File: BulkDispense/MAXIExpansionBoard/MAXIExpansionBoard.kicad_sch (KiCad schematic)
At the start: 25 parts, among them J1 BS1~4, J10 FS3, J11 R6~R7, J12 R8~R9, J13 OS1~4, J14 WV1~2, J15 FS2, J16 FS4, J17 Analog Inputs, J18 Digital IN + R0~R4, J19 Digital Outputs, J2 MV1~4, J20 R4~R9, J21 Flow Sensors, J3 WB/WL, J4 PS/PCV, J5 Screw_Terminal_01x02, J6 R0~R1, J7 R2~R3, J8 R4~R5, J9 FS1

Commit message: Design Overhaul
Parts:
- removed J1: BS1~4, PartsLibrary:CONN_37204-62A3-004PL_3MM, symbol Connector:Conn_01x04_Socket
- removed J10: FS3, PartsLibrary:CONN_37204-62A3-004PL_3MM, symbol Connector:Conn_01x04_Socket
- removed J13: OS1~4, PartsLibrary:CONN_37204-62A3-004PL_3MM, symbol Connector:Conn_01x04_Socket
- removed J14: WV1~2, PartsLibrary:3720362A3003PL, symbol Connector:Conn_01x03_Socket
- removed J17: Analog Inputs, PartsLibrary:CONN_37212-62M3-003PL_3MM, symbol Connector:Conn_01x12_Socket
- removed J19: Digital Outputs, PartsLibrary:CONN_37212-62M3-003PL_3MM, symbol Connector:Conn_01x12_Socket
- removed J2: MV1~4, PartsLibrary:CONN_37204-62A3-004PL_3MM, symbol Connector:Conn_01x04_Socket
- removed J3: WB/WL, PartsLibrary:CONN_37204-62A3-004PL_3MM, symbol Connector:Conn_01x04_Socket
- removed J4: PS/PCV, PartsLibrary:3720362A3003PL, symbol Connector:Conn_01x03_Socket
- removed J5: Screw_Terminal_01x02, PartsLibrary:691137710002, symbol Connector:Screw_Terminal_01x02
- removed J6: R0~R1, PartsLibrary:CONN_37204-62A3-004PL_3MM, symbol Connector:Conn_01x04_Socket
- removed J7: R2~R3, PartsLibrary:CONN_37204-62A3-004PL_3MM, symbol Connector:Conn_01x04_Socket
- removed J8: R4~R5, PartsLibrary:CONN_37204-62A3-004PL_3MM, symbol Connector:Conn_01x04_Socket
- added H10, H5, H6, H7, H8, H9: MountingHole, MountingHole:MountingHole_2.5mm, symbol Mechanical:MountingHole
- added H11: MountingHole, MountingHole:MountingHole_3.2mm_M3, symbol Mechanical:MountingHole
- added J13: PS/PCV, PartsLibrary:3720362A3003PL, symbol Connector:Conn_01x03_Socket
- added J14: RV1&2, PartsLibrary:CONN_37204-62A3-004PL_3MM, symbol Connector:Conn_01x04_Socket
- added J17: FS3, PartsLibrary:CONN_37204-62A3-004PL_3MM, symbol Connector:Conn_01x04_Socket
- added J18: WB-MV1~4, PartsLibrary:CONN_37204-62A3-004PL_3MM, symbol Connector:Conn_01x04_Socket
- added J19: FS2, PartsLibrary:CONN_37204-62A3-004PL_3MM, symbol Connector:Conn_01x04_Socket
- added J2: BS1~4, PartsLibrary:CONN_37212-62M3-003PL_3MM, symbol Connector:Conn_01x12_Socket
- added J20: FS4, PartsLibrary:CONN_37204-62A3-004PL_3MM, symbol Connector:Conn_01x04_Socket
- added J21: BS1~4, PartsLibrary:CONN_37204-62A3-004PL_3MM, symbol Connector:Conn_01x04_Socket
- added J22: OS1~4, PartsLibrary:CONN_37204-62A3-004PL_3MM, symbol Connector:Conn_01x04_Socket
- added J23: WB-MV5~6, PartsLibrary:CONN_37204-62A3-004PL_3MM, symbol Connector:Conn_01x04_Socket
- added J3: Screw_Terminal_01x02, PartsLibrary:691137710002, symbol Connector:Screw_Terminal_01x02
- added J4: DigitalOUT 0~3, PartsLibrary:CONN_37204-62A3-004PL_3MM, symbol Connector:Conn_01x04_Socket
- added J5: DigitalOUT 4~7, PartsLibrary:CONN_37204-62A3-004PL_3MM, symbol Connector:Conn_01x04_Socket
- added J6: OS1~4, PartsLibrary:CONN_37212-62M3-003PL_3MM, symbol Connector:Conn_01x12_Socket
- added J8: Fan PWR, PartsLibrary:3720362A3003PL, symbol Connector:Conn_01x03_Socket
- H1, H2, H3, H4: footprint MountingHole:MountingHole_2.2mm_M2 -> MountingHole:MountingHole_3.2mm_M3
- J1: renamed from J18; value Digital IN + R0~R4 -> R0~R5
- J10: renamed from J21; value Flow Sensors -> FS2~FS4
- J11: value R6~R7 -> MV1~4
- J12: value R8~R9 -> WB/WL
- J15: value FS2 -> RV3&4
- J16: value FS4 -> FS1
- J7: renamed from J20; value R4~R9 -> AnalogIOs
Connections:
- net +24V: now also J7.10 (Pin_10), J2.1 (Pin_1), J2.10 (Pin_10), J2.4 (Pin_4), J2.7 (Pin_7), J3.1 (Pin_1), J6.1 (Pin_1), J6.10 (Pin_10), J6.4 (Pin_4), J6.7 (Pin_7), J8.1 (Pin_1)
- net AI0: now also J2.3 (Pin_3), J21.1 (Pin_1)
- net AI1: now also J2.6 (Pin_6), J21.2 (Pin_2)
- net AI12: now also J7.5 (Pin_5), J13.1 (Pin_1)
- net AI13: now also J7.6 (Pin_6), J13.2 (Pin_2)
- net AI2: now also J2.9 (Pin_9), J21.3 (Pin_3)
- net AI3: now also J2.12 (Pin_12), J21.4 (Pin_4)
- net AI4: now also J12.1 (Pin_1), J7.1 (Pin_1)
- net AI5: now also J12.2 (Pin_2), J7.2 (Pin_2)
- net AI6: now also J12.3 (Pin_3), J7.3 (Pin_3)
- net AI7: now also J12.4 (Pin_4), J7.4 (Pin_4)
- net AO0: now also J7.8 (Pin_8), J13.3 (Pin_3); no longer J10.11 (Pin_11)
- net DI0: now also J22.1 (Pin_1), J6.3 (Pin_3); no longer J1.1 (Pin_1)
- net DI1: now also J22.2 (Pin_2), J6.6 (Pin_6); no longer J1.2 (Pin_2)
- net DI2: now also J22.3 (Pin_3), J6.9 (Pin_9); no longer J1.3 (Pin_3)
- net DI3: now also J22.4 (Pin_4), J6.12 (Pin_12); no longer J1.4 (Pin_4)
- net DO0: now also J11.1 (Pin_1), J4.1 (Pin_1)
- net DO1: now also J11.2 (Pin_2), J4.2 (Pin_2)
- net DO2: now also J11.3 (Pin_3), J4.3 (Pin_3)
- net DO3: now also J11.4 (Pin_4), J4.4 (Pin_4)
- net FS1-1: now also J16.1 (Pin_1)
- net FS1-2: now also J16.2 (Pin_2)
- net FS1-3: now also J16.3 (Pin_3)
- net FS1-4: now also J16.4 (Pin_4)
- net FS2-1: now also J10.1 (Pin_1), J19.1 (Pin_1); no longer J15.1 (Pin_1)
- net FS2-2: now also J10.2 (Pin_2), J19.2 (Pin_2); no longer J15.2 (Pin_2)
- net FS2-3: now also J10.3 (Pin_3), J19.3 (Pin_3); no longer J10.1 (Pin_1), J15.3 (Pin_3)
- net FS2-4: now also J10.4 (Pin_4), J19.4 (Pin_4); no longer J10.2 (Pin_2), J15.4 (Pin_4)
- net FS3-1: now also J10.5 (Pin_5), J17.1 (Pin_1); no longer J10.3 (Pin_3)
- net FS3-2: now also J10.6 (Pin_6), J17.2 (Pin_2); no longer J10.4 (Pin_4)
- net FS3-3: now also J10.7 (Pin_7), J17.3 (Pin_3); no longer J10.5 (Pin_5)
- net FS3-4: now also J10.8 (Pin_8), J17.4 (Pin_4); no longer J10.6 (Pin_6)
- net FS4-1: now also J10.9 (Pin_9), J20.1 (Pin_1); no longer J10.7 (Pin_7), J16.1 (Pin_1)
- net FS4-2: now also J10.10 (Pin_10), J20.2 (Pin_2); no longer J10.8 (Pin_8), J16.2 (Pin_2)
- net FS4-3: now also J10.11 (Pin_11), J20.3 (Pin_3); no longer J10.9 (Pin_9), J16.3 (Pin_3)
- net FS4-4: now also J10.12 (Pin_12), J20.4 (Pin_4); no longer J10.10 (Pin_10), J16.4 (Pin_4)
- net GND: now also J7.12 (Pin_12), J2.11 (Pin_11), J2.2 (Pin_2), J2.5 (Pin_5), J2.8 (Pin_8), J3.2 (Pin_2), J6.11 (Pin_11), J6.2 (Pin_2), J6.5 (Pin_5), J6.8 (Pin_8)
- net R0_IN: now also J1.1 (Pin_1), J14.2 (Pin_2); no longer J1.5 (Pin_5)
- net R0_OUT: now also J1.7 (Pin_7), J14.1 (Pin_1); no longer J1.9 (Pin_9)
- net R1_IN: now also J1.2 (Pin_2), J14.4 (Pin_4); no longer J1.6 (Pin_6)
- net R1_OUT: now also J1.8 (Pin_8), J14.3 (Pin_3); no longer J1.10 (Pin_10)
- net R2_IN: now also J1.3 (Pin_3), J15.2 (Pin_2); no longer J1.7 (Pin_7)
- net R2_OUT: now also J1.9 (Pin_9), J15.1 (Pin_1); no longer J1.11 (Pin_11)
- net R3_IN: now also J1.4 (Pin_4), J15.4 (Pin_4); no longer J1.8 (Pin_8)
- net R3_OUT: now also J1.10 (Pin_10), J15.3 (Pin_3); no longer J1.12 (Pin_12)
- net R4_IN: now also J1.5 (Pin_5), J23.2 (Pin_2); no longer J7.1 (Pin_1)
- net R4_OUT: now also J1.11 (Pin_11), J23.1 (Pin_1); no longer J7.7 (Pin_7)
- net R5_IN: now also J1.6 (Pin_6), J23.4 (Pin_4); no longer J7.2 (Pin_2)
- net R5_OUT: now also J1.12 (Pin_12), J23.3 (Pin_3); no longer J7.8 (Pin_8)
- net R6_OUT: now also J8.2 (Pin_2); no longer J11.1 (Pin_1), J7.9 (Pin_9)
- removed net R6_IN: J11.2 (Pin_2), J7.3 (Pin_3)
- removed net R7_IN: J11.4 (Pin_4), J7.4 (Pin_4)
- removed net R7_OUT: J11.3 (Pin_3), J7.10 (Pin_10)
- removed net R8_IN: J12.2 (Pin_2), J7.5 (Pin_5)
- net R8_OUT: no longer names the net of J7.11 (Pin_11)
- net R8_OUT: no longer J12.1 (Pin_1)
- removed net R9_IN: J12.4 (Pin_4), J7.6 (Pin_6)
- removed net R9_OUT: J12.3 (Pin_3), J7.12 (Pin_12)
- new net DO4: J18.1 (Pin_1), J5.1 (Pin_1)
- new net DO5: J18.2 (Pin_2), J5.2 (Pin_2)
- new net DO6: J18.3 (Pin_3), J5.3 (Pin_3)
- new net DO7: J18.4 (Pin_4), J5.4 (Pin_4)
- no-connect marks 2 -> 4
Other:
- note added: "Controllino Inbound - From Plumbing"
- note added: "Misc. Connections"
- note added: "RV1"
- note added: "RV2"
- note added: "RV3"
- note added: "RV4"
- note added: "Sensor Connects to I2C Bus"
- note added: "Signal Connection to Controllino"
- note added: "WB-MV1"
- note added: "WB-MV2"
- note added: "WB-MV3"
- note added: "WB-MV4"
- note added: "WB-MV5"
- note added: "WB-MV6"
- note removed: "Controllino Inbound"
- note removed: "Relays"
- note removed: "WV1"
- note removed: "WV2"
- moved on the sheet: J1, J10, J7

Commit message: Add latest design
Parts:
- added H12, H13, H14, H15: MountingHole, MountingHole:MountingHole_2.5mm, symbol Mechanical:MountingHole
- added J24: LDS, PartsLibrary:CONN_37204-62A3-004PL_3MM, symbol Connector:Conn_01x04_Socket
- J1, J10, J2, J6, J7: MPN (none) -> 37212-62M3-003PL; Manufacturer (none) -> 3M
- J11, J12, J14, J15, J16, J17, J18, J19, J20, J21, J22, J23, J4, J5, J9: MPN (none) -> 37204-62A3-004PL; Manufacturer (none) -> 3M
- J13, J8: footprint PartsLibrary:3720362A3003PL -> PartsLibrary:CONN_37203-62A3-003PL_3MM; MPN (none) -> 37203-62A3-003PL; Manufacturer (none) -> 3M
- J3: MPN (none) -> 691137710002; Manufacturer (none) -> Würth Elektronik
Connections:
- net +24V: now also J7.11 (Pin_11); no longer J7.10 (Pin_10)
- net AO0: now also J7.7 (Pin_7); no longer J7.8 (Pin_8)
- net LDS-GND: now reaches J7.9 (Pin_9)
- net LDS-GND: now also J24.2 (Pin_2)
- new net LDS: J24.3 (Pin_3), J7.10 (Pin_10)
- new net LDS-5V: J24.1 (Pin_1), J7.8 (Pin_8)
- no-connect marks 4 -> 2

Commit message: Add updated layout
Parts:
- removed J13: PS/PCV, PartsLibrary:CONN_37203-62A3-003PL_3MM, symbol Connector:Conn_01x03_Socket
- removed J8: Fan PWR, PartsLibrary:CONN_37203-62A3-003PL_3MM, symbol Connector:Conn_01x03_Socket
- added J13: PS/PCV, PartsLibrary:CONN_37204-62A3-004PL_3MM, symbol Connector:Conn_01x04_Socket
- added J8: Fan PWR, PartsLibrary:CONN_37204-62A3-004PL_3MM, symbol Connector:Conn_01x04_Socket
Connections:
- net +24V: now also J8.1 (Pin_1)
- net AI12: now also J13.1 (Pin_1)
- net AI13: now also J13.2 (Pin_2)
- net AO0: now also J13.3 (Pin_3)
- net R6_OUT: now also J8.3 (Pin_3)
- no-connect marks 2 -> 4

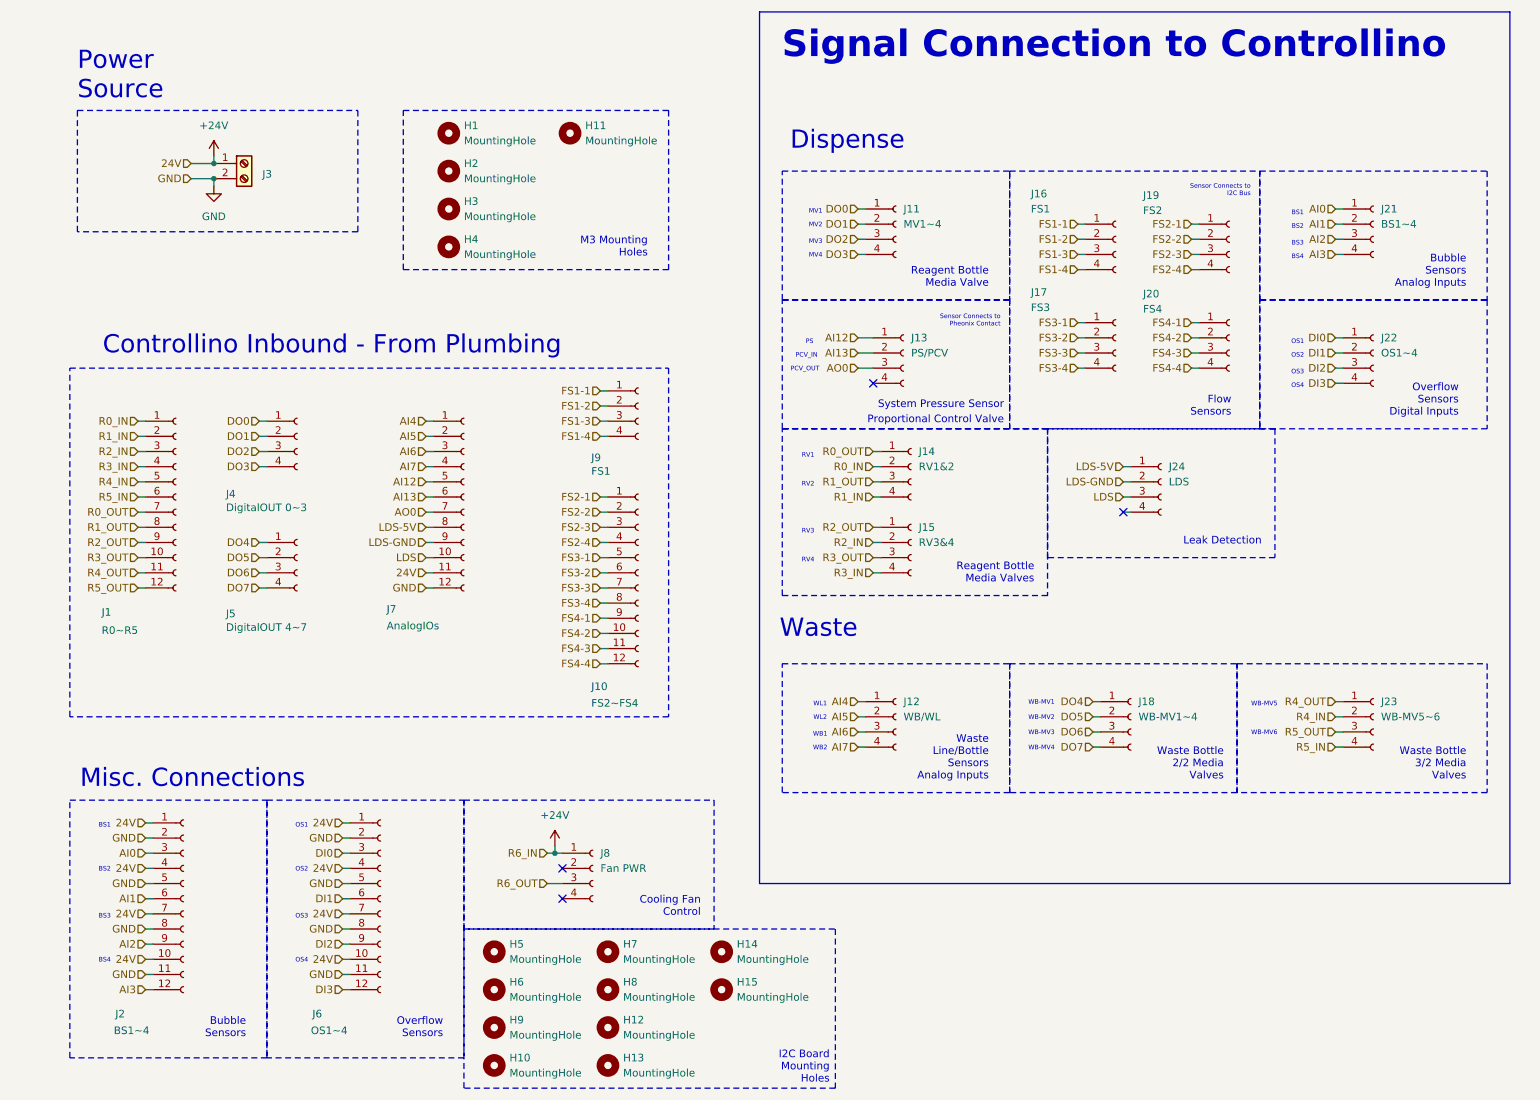
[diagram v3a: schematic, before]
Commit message: Add PCB Revisions
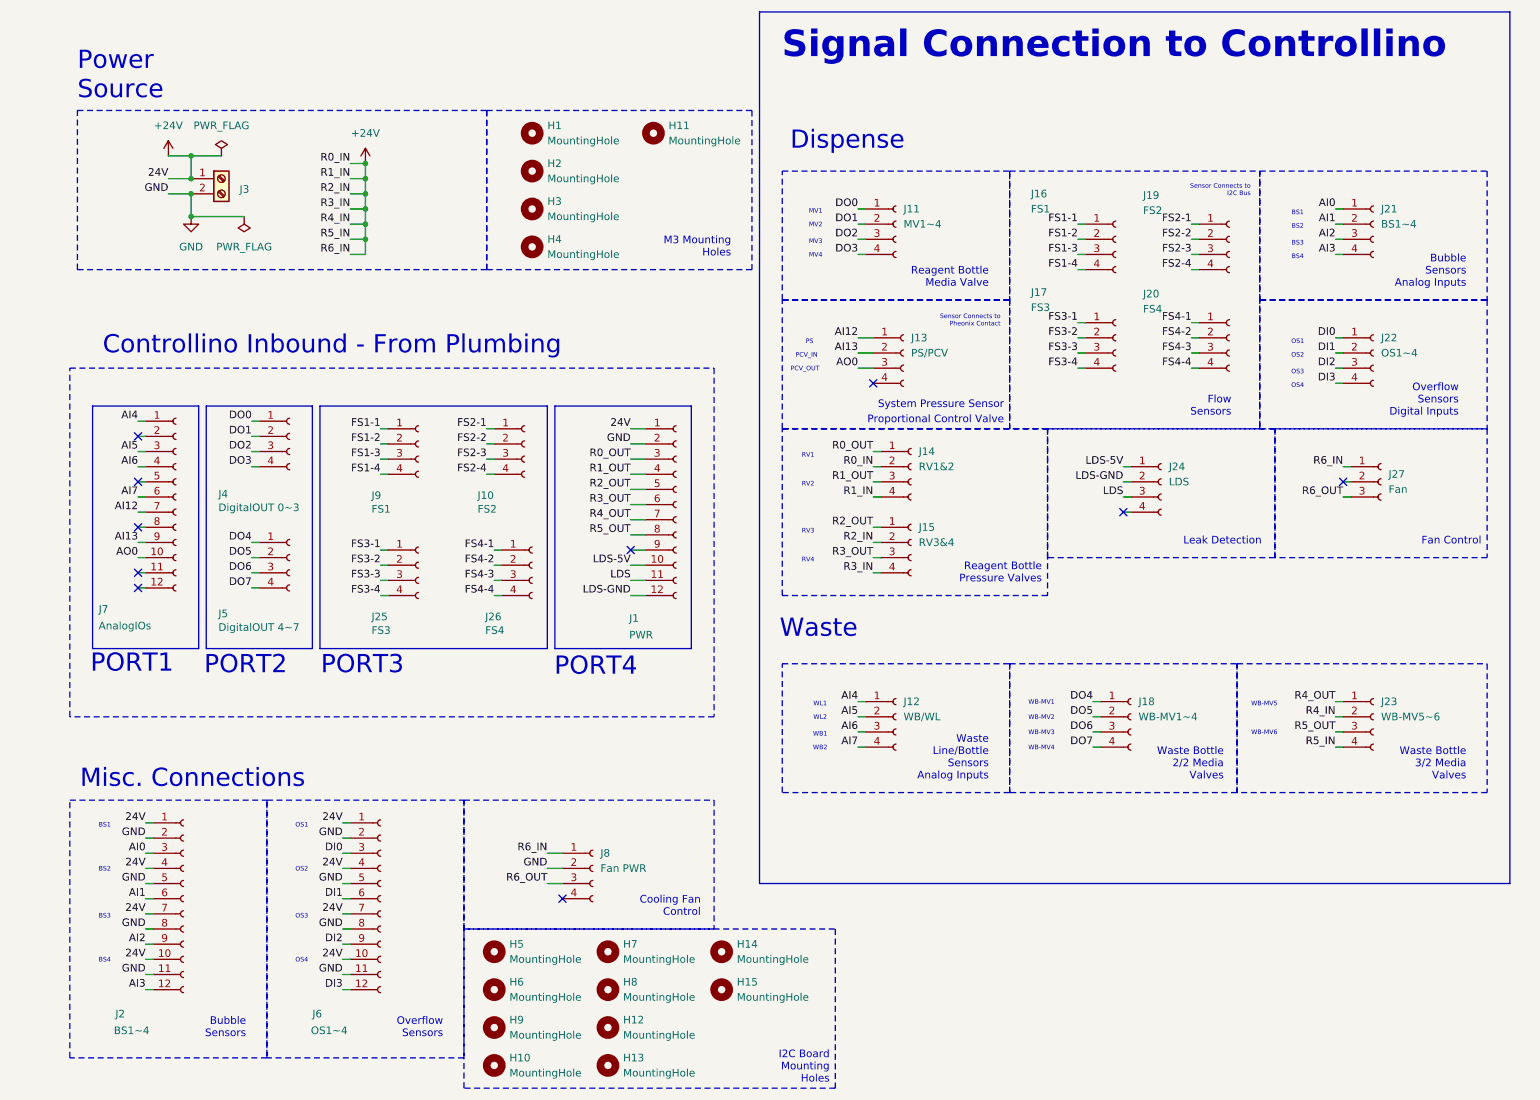
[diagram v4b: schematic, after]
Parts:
- removed J10: FS2~FS4, PartsLibrary:CONN_37212-62M3-003PL_3MM, symbol Connector:Conn_01x12_Socket
- added J10: FS2, PartsLibrary:CONN_37204-62A3-004PL_3MM, symbol Connector:Conn_01x04_Socket
- added J25: FS3, PartsLibrary:CONN_37204-62A3-004PL_3MM, symbol Connector:Conn_01x04_Socket
- added J26: FS4, PartsLibrary:CONN_37204-62A3-004PL_3MM, symbol Connector:Conn_01x04_Socket
- added J27: Fan, symbol Connector:Conn_01x03_Socket
- J1: value R0~R5 -> PWR
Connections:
- net R0_IN is gone; now on net +24V: J1.1 (Pin_1), J14.2 (Pin_2)
- net +24V: now also J14.4 (Pin_4), J15.2 (Pin_2), J15.4 (Pin_4), J23.2 (Pin_2), J23.4 (Pin_4), J27.1 (Pin_1); no longer J7.11 (Pin_11)
- net AI12: now also J7.7 (Pin_7); no longer J7.5 (Pin_5)
- net AI13: now also J7.9 (Pin_9); no longer J7.6 (Pin_6)
- net AI5: now also J7.3 (Pin_3); no longer J7.2 (Pin_2)
- net AI6: now also J7.4 (Pin_4); no longer J7.3 (Pin_3)
- net AI7: now also J7.6 (Pin_6); no longer J7.4 (Pin_4)
- net AO0: now also J7.10 (Pin_10); no longer J7.7 (Pin_7)
- net FS2-1: now also J10.1 (Pin_1)
- net FS2-2: now also J10.2 (Pin_2)
- net FS2-3: now also J10.3 (Pin_3)
- net FS2-4: now also J10.4 (Pin_4)
- net FS3-1: now also J25.1 (Pin_1)
- net FS3-2: now also J25.2 (Pin_2)
- net FS3-3: now also J25.3 (Pin_3)
- net FS3-4: now also J25.4 (Pin_4)
- net FS4-1: now also J26.1 (Pin_1)
- net FS4-2: now also J26.2 (Pin_2)
- net FS4-3: now also J26.3 (Pin_3)
- net FS4-4: now also J26.4 (Pin_4)
- net GND: now also J1.2 (Pin_2), J8.2 (Pin_2); no longer J7.12 (Pin_12)
- net LDS: now also J1.11 (Pin_11); no longer J7.10 (Pin_10)
- net LDS-5V: now also J1.10 (Pin_10); no longer J7.8 (Pin_8)
- net LDS-GND: now also J1.12 (Pin_12); no longer J7.9 (Pin_9)
- net R0_OUT: now also J1.3 (Pin_3); no longer J1.7 (Pin_7)
- net R1_OUT: now also J1.4 (Pin_4); no longer J1.8 (Pin_8)
- net R2_OUT: now also J1.5 (Pin_5); no longer J1.9 (Pin_9)
- net R3_OUT: now also J1.6 (Pin_6); no longer J1.10 (Pin_10)
- net R4_OUT: now also J1.7 (Pin_7); no longer J1.11 (Pin_11)
- net R5_OUT: now also J1.8 (Pin_8); no longer J1.12 (Pin_12)
- net R6_OUT: now also J27.3 (Pin_3)
- removed net R1_IN: J1.2 (Pin_2), J14.4 (Pin_4)
- removed net R2_IN: J1.3 (Pin_3), J15.2 (Pin_2)
- removed net R3_IN: J1.4 (Pin_4), J15.4 (Pin_4)
- removed net R4_IN: J1.5 (Pin_5), J23.2 (Pin_2)
- removed net R5_IN: J1.6 (Pin_6), J23.4 (Pin_4)
- no-connect marks 4 -> 10
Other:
- note added: "PORT1"
- note added: "PORT2"
- note added: "PORT3"
- note added: "PORT4"
- moved on the sheet: H1, H11, H2, H3, H4, J3

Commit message: PCB Changes
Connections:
- net LDS: now also J7.12 (Pin_12); no longer J1.11 (Pin_11)
- net LDS-5V: no longer J1.10 (Pin_10)
- net LDS-GND: no longer J1.12 (Pin_12)
- no-connect marks 10 -> 12
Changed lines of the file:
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@@
+	)
+	(no_connect
+		(at 125.73 109.22)
 	)
 	(no_connect
@@
 	)
 	(no_connect
+		(at 125.73 111.76)
+	)
+	(no_connect
 		(at 166.37 78.74)
-	)
-	(no_connect
-		(at 43.18 113.03)
 	)
 	(no_connect
@@
 	)
 	(no_connect
+		(at 125.73 114.3)
+	)
+	(no_connect
 		(at 43.18 95.25)
 	)
@@
 		)
 	)
-	(label "LDS"
-		(at 125.73 111.76 180)
-		(effects
-			(font
-				(size 1.27 1.27)
-			)
-			(justify right bottom)
-		)
-	)
 	(label "FS3-3"
 		(at 83.82 111.76 180)
@@
 		)
 	)
-	(label "LDS-5V"
-		(at 125.73 109.22 180)
-		(effects
-			(font
-				(size 1.27 1.27)
-			)
-			(justify right bottom)
-		)
-	)
 	(label "FS1-3"
 		(at 200.66 57.15 180)
@@
 		)
 	)
-	(label "LDS-GND"
-		(at 125.73 114.3 180)
-		(effects
-			(font
-				(size 1.27 1.27)
-			)
-			(justify right bottom)
-		)
-	)
 	(label "AI0"
 		(at 44.45 157.48 180)
@@
 		(effects
 			(font
+				(size 1.27 1.27)
+			)
+			(justify right bottom)
+		)
+	)
+	(label "LDS"
+		(at 43.18 113.03 180)
+		(effects
+			(font

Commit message: Final Design Changes for Both Boards
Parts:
- removed J1: PWR, PartsLibrary:CONN_37212-62M3-003PL_3MM, symbol Connector:Conn_01x12_Socket
- removed J10, J19: FS2, PartsLibrary:CONN_37204-62A3-004PL_3MM, symbol Connector:Conn_01x04_Socket
- removed J14: RV1&2, PartsLibrary:CONN_37204-62A3-004PL_3MM, symbol Connector:Conn_01x04_Socket
- removed J15: RV3&4, PartsLibrary:CONN_37204-62A3-004PL_3MM, symbol Connector:Conn_01x04_Socket
- removed J16, J9: FS1, PartsLibrary:CONN_37204-62A3-004PL_3MM, symbol Connector:Conn_01x04_Socket
- removed J17, J25: FS3, PartsLibrary:CONN_37204-62A3-004PL_3MM, symbol Connector:Conn_01x04_Socket
- removed J20, J26: FS4, PartsLibrary:CONN_37204-62A3-004PL_3MM, symbol Connector:Conn_01x04_Socket
- removed J23: WB-MV5~6, PartsLibrary:CONN_37204-62A3-004PL_3MM, symbol Connector:Conn_01x04_Socket
- removed J24: LDS, PartsLibrary:CONN_37204-62A3-004PL_3MM, symbol Connector:Conn_01x04_Socket
- removed J4: DigitalOUT 0~3, PartsLibrary:CONN_37204-62A3-004PL_3MM, symbol Connector:Conn_01x04_Socket
- removed J5: DigitalOUT 4~7, PartsLibrary:CONN_37204-62A3-004PL_3MM, symbol Connector:Conn_01x04_Socket
- removed J7: AnalogIOs, PartsLibrary:CONN_37212-62M3-003PL_3MM, symbol Connector:Conn_01x12_Socket
- removed J8: Fan PWR, PartsLibrary:CONN_37204-62A3-004PL_3MM, symbol Connector:Conn_01x04_Socket
- added J10: Signal, PartsLibrary:CONN26_D13-ST-BK_SUL, symbol Connector_Generic:Conn_01x26
- added J11: RV3, PartsLibrary:CONN_37203-62A3-003PL_3MM, symbol Connector:Conn_01x03_Socket
- added J12: RV4, PartsLibrary:CONN_37203-62A3-003PL_3MM, symbol Connector:Conn_01x03_Socket
- added J13: WB-MV5, PartsLibrary:CONN_37203-62A3-003PL_3MM, symbol Connector:Conn_01x03_Socket
- added J16: WB-MV6, PartsLibrary:CONN_37203-62A3-003PL_3MM, symbol Connector:Conn_01x03_Socket
- added J17: Fan PWR, PartsLibrary:CONN_37203-62A3-003PL_3MM, symbol Connector:Conn_01x03_Socket
- added J4: I2C, PartsLibrary:CONN_37203-62A3-003PL_3MM, symbol Connector:Conn_01x03_Socket
- added J8: RV1, PartsLibrary:CONN_37203-62A3-003PL_3MM, symbol Connector:Conn_01x03_Socket
- added J9: RV2, PartsLibrary:CONN_37203-62A3-003PL_3MM, symbol Connector:Conn_01x03_Socket
- J5: renamed from J13; value PS/PCV -> PS/PCV/LDS
- J7: renamed from J27; footprint (none) -> PartsLibrary:CONN_37203-62A3-003PL_3MM
- renumbered H9 to H10, H10 to H11, H11 to H2, H2 to H3, H3 to H4, H4 to H5, H5 to H6, H6 to H8, H8 to H9, J3 to J1, J12 to J14, J18 to J15, J2 to J18, J6 to J19, J11 to J2, J21 to J3, J22 to J6
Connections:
- net +24V: now also J10.1 (Pin_1), J11.1 (Pin_1), J12.1 (Pin_1), J13.1 (Pin_1), J16.1 (Pin_1), J8.1 (Pin_1), J9.1 (Pin_1)
- net AI12: now also J10.10 (Pin_10)
- net AI13: now also J10.11 (Pin_11)
- net AI4: now also J10.6 (Pin_6)
- net AI5: now also J10.7 (Pin_7)
- net AI6: now also J10.8 (Pin_8)
- net AI7: now also J10.9 (Pin_9)
- net AO0: now also J10.12 (Pin_12)
- net DO0: now also J10.19 (Pin_19)
- net DO1: now also J10.20 (Pin_20)
- net DO2: now also J10.21 (Pin_21)
- net DO3: now also J10.22 (Pin_22)
- net DO4: now also J10.23 (Pin_23)
- net DO5: now also J10.24 (Pin_24)
- net DO6: now also J10.25 (Pin_25)
- net DO7: now also J10.26 (Pin_26)
- net GND: now also J10.2 (Pin_2), J17.3 (Pin_3)
- net LDS: now also J5.4 (Pin_4), J10.5 (Pin_5)
- net R0_OUT: now also J10.13 (Pin_13), J8.3 (Pin_3)
- net R1_OUT: now also J10.14 (Pin_14), J9.3 (Pin_3)
- net R2_OUT: now also J10.15 (Pin_15), J11.3 (Pin_3)
- net R3_OUT: now also J10.16 (Pin_16), J12.3 (Pin_3)
- net R4_OUT: now also J10.17 (Pin_17), J13.3 (Pin_3)
- net R5_OUT: now also J10.18 (Pin_18), J16.3 (Pin_3)
- net R6_OUT: now also J17.1 (Pin_1)
- new net SCL: J10.4 (Pin_4), J4.1 (Pin_1)
- new net SDA: J10.3 (Pin_3), J4.3 (Pin_3)
- no-connect marks 12 -> 9
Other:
- note added: "Connects to Controllino I2C Bus"
- note removed: "Misc. Connections"
- note removed: "PORT1"
- note removed: "PORT2"
- note removed: "PORT3"
- note removed: "PORT4"
- note removed: "RV1"
- note removed: "RV2"
- note removed: "RV3"
- note removed: "RV4"
- note removed: "Sensor Connects to I2C Bus"
- note removed: "WB-MV5"
- note removed: "WB-MV6"
- moved on the sheet: H10, H11, H6, H7, H8, H9, J18, J19, J3, J6, J7
